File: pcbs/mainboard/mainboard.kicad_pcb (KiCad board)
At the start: 4 copper layers, 49 parts, among them J1 USB_B_Micro, J10 STAT_LED, J11 nReset_Button, J12 VBUS, J2 key_row_0, J3 key_row_1, J4 key_row_2, J5 ICSP, J6 JTAG, J7 Crank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

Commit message: Add first draft of mainboard routing
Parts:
- moved J10 40.7 mm to (116.0, 80.0)
- moved J11 40.7 mm to (153.0, 97.0)
- moved C5 20.7 mm to (122.5, 95.9)
- moved C10 13.0 mm to (106.5, 101.2), turned to 270 degrees
- moved R4 8.45 mm to (140.4, 106.8), turned to 270 degrees
- moved C13 5.91 mm to (137.9, 90.1), turned to 0 degrees
- moved J5 5.79 mm to (139.5, 110.2), turned to 270 degrees
- moved R1 4.82 mm to (155.0, 113.0), turned to 180 degrees
- moved C5 4.61 mm to (114.0, 85.3)
- moved C11 3.57 mm to (120.5, 110.5), turned to 90 degrees
- moved FB1 3.25 mm to (120.8, 114.0)
- moved L1 2.34 mm to (138.1, 86.8), turned to 270 degrees
- moved U2 2.26 mm to (130.4, 111.0)
- moved H1 2.00 mm to (128.5, 34.0)
- moved J1 1.65 mm to (129.0, 118.8)
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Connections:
- net Net-(R2-Pad2) renamed /D+
- net Net-(R3-Pad1) renamed /D-
- U4 pad 12: MISO -> /key_bus0
- U4 pad 13: MOSI -> SCK
- U4 pad 14: SCK -> MOSI
- U4 pad 16: /key_bus0 -> MISO
- U4 pad 18: /key_sel0 -> /key_sel1
- U4 pad 19: /key_sel1 -> /key_sel0
- U4 pad 40: key_row0_7 -> key_row0_6
- U4 pad 41: key_row0_6 -> key_row0_7
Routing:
- net GPIO7: track 0.00 -> 111.1 mm, vias 0 -> 2
- net GPIO6_HWB: track 0.00 -> 102.8 mm, vias 0 -> 1
- net key_row0_0: track 0.00 -> 86.6 mm
- net key_row0_1: track 0.00 -> 78.6 mm
- net VBUS: track 0.00 -> 75.6 mm, vias 0 -> 3
- net key_row1_0: track 0.00 -> 71.8 mm
- net key_row0_2: track 0.00 -> 71.2 mm
- net key_row2_0: track 0.00 -> 69.1 mm
- net STAT_LED: track 0.00 -> 65.6 mm, vias 0 -> 3
- net key_row1_1: track 0.00 -> 64.1 mm
- net key_row2_1: track 0.00 -> 63.6 mm
- net key_row2_2: track 0.00 -> 58.4 mm
- net GPIO5: track 0.00 -> 57.6 mm
- net key_row1_2: track 0.00 -> 57.4 mm
- net key_row0_3: track 0.00 -> 56.7 mm
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- added copper zone on In2.Cu, net +3V3
- added copper zone on In1.Cu, net GND
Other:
- board outline added: 59 x 93 mm

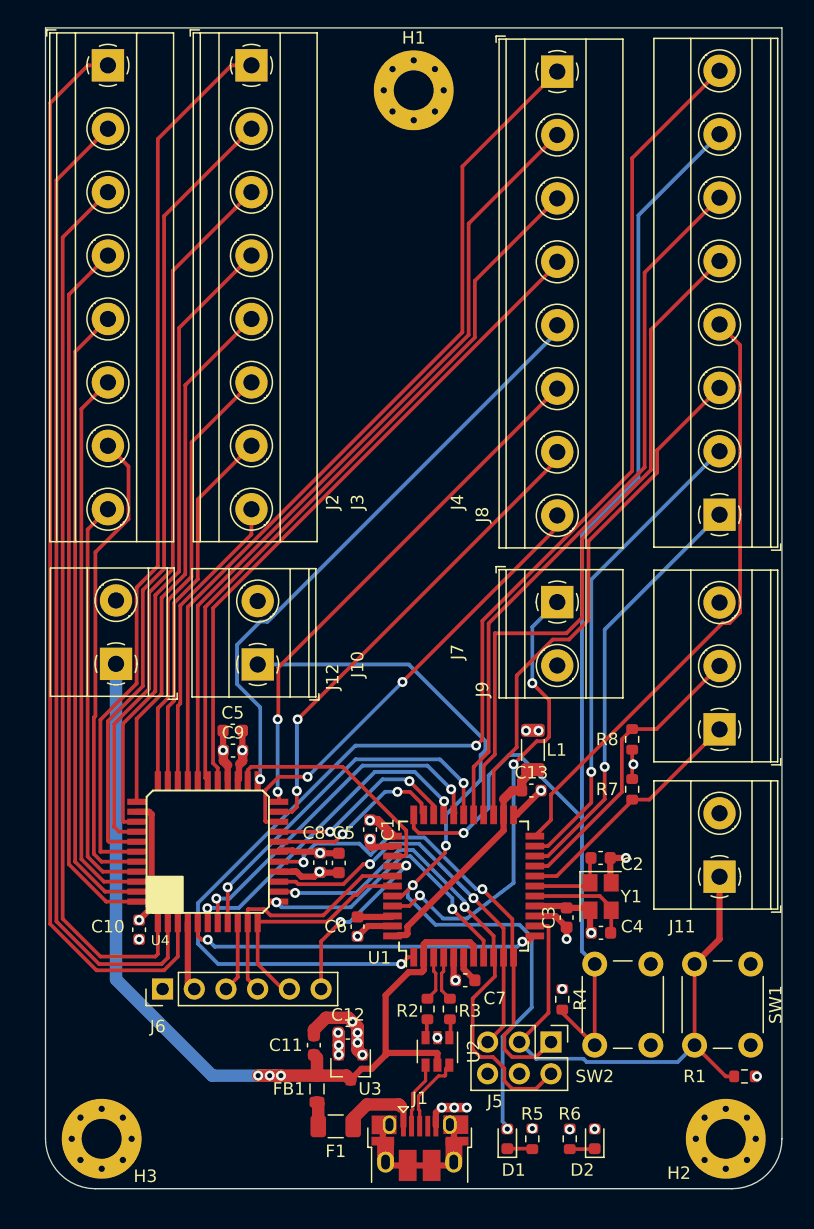
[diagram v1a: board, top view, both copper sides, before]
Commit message: Improve routing around 32U4
Move some pin assignments round on the 32U4 to simplify routing
to the lower-priority IO.
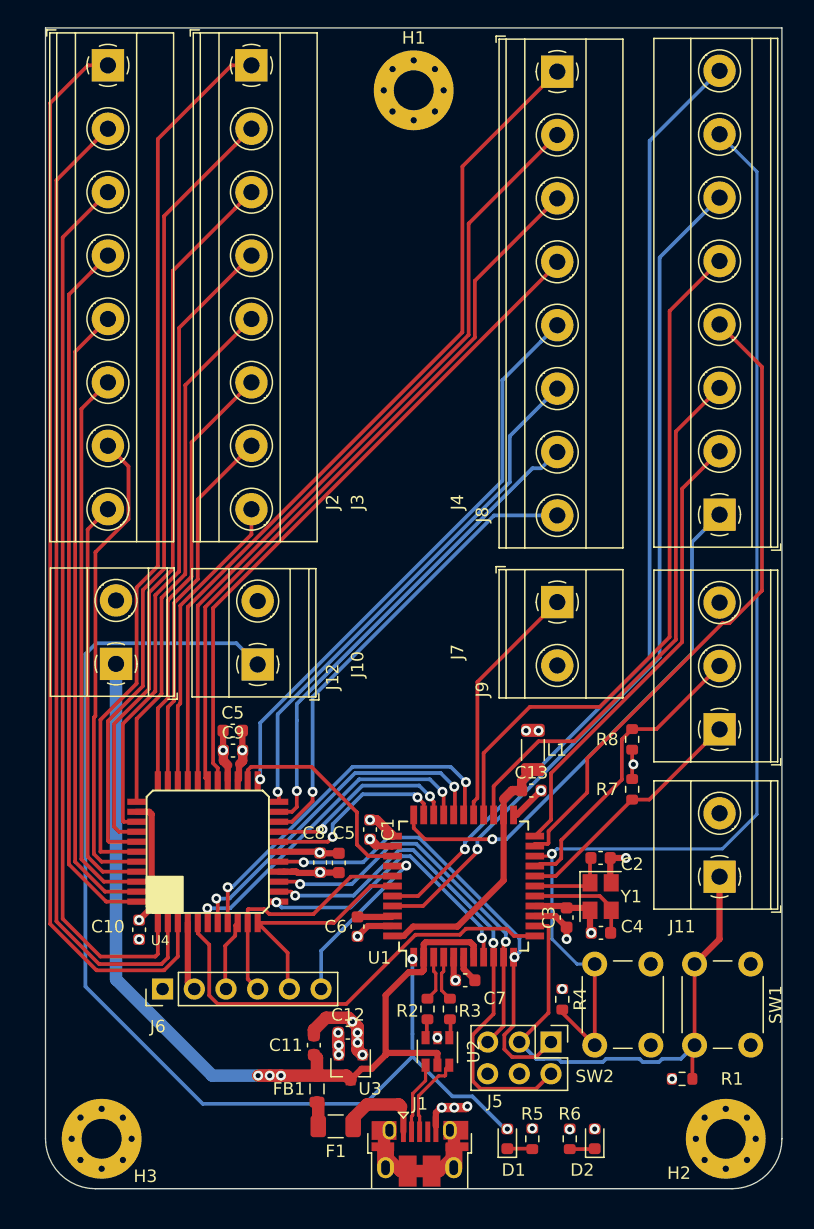
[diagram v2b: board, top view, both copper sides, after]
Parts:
- moved R1 5.00 mm to (150.0, 113.2), turned to 0 degrees
- moved J1 0.45 mm to (129.0, 119.2)
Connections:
- U1 pad 1: GPIO7 -> STAT_LED
- U1 pad 20: GPIO0 -> GPIO6_HWB
- U1 pad 21: GPIO1 -> GPIO3
- U1 pad 22: GPIO3 -> GPIO1
- U1 pad 27: GPIO5 -> CRANK_V_IN
- U1 pad 33: GPIO6_HWB -> GPIO0
- U1 pad 40: STAT_LED -> GPIO7
- U1 pad 41: CRANK_V_IN -> GPIO5
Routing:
- net GPIO7: track 111.1 -> 78.2 mm, vias 2 -> 1
- net STAT_LED: track 65.6 -> 91.2 mm, vias 3 -> 2
- net CRANK_V_IN: track 37.2 -> 19.8 mm, vias 3 -> 0
- net GPIO5: track 57.6 -> 69.0 mm, vias 0 -> 1
- net GPIO0: track 34.1 -> 41.9 mm
- net /key_bus7: track 28.8 -> 35.3 mm, vias 2 -> 0
- net GPIO6_HWB: track 102.8 -> 96.4 mm
- net GPIO3: track 48.8 -> 51.7 mm
- net Net-(J1-Pad6): track 9.36 -> 11.7 mm
- net +3.3VA: track 19.0 -> 21.0 mm
- net 32U4_TDI: track 19.0 -> 17.0 mm
- net key_row2_4: track 48.4 -> 46.5 mm
- net GPIO1: track 38.4 -> 37.0 mm, vias 1 -> 0
- net nReset_32U4: track 45.1 -> 43.9 mm
- net MISO: track 38.6 -> 37.4 mm
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
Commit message: Fix vias placed under SMD pads
Move vias out from underneath SMD pads to prevent solder paste
being sucked into them during manufacture.

Redo power layout to accomadate large areas of vias to power planes.
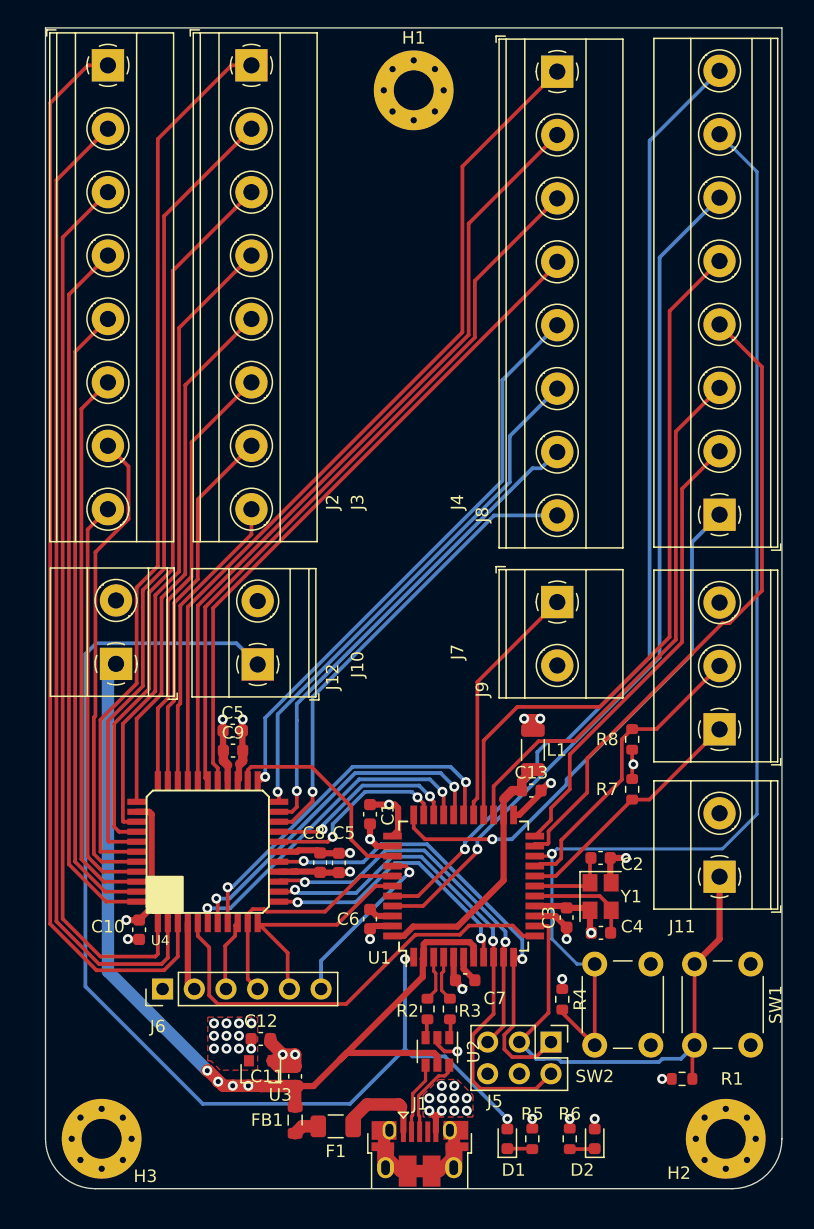
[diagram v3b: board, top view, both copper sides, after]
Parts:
- moved U3 7.21 mm to (116.2, 112.8)
- moved C12 6.99 mm to (116.2, 110.0)
- moved FB1 3.05 mm to (119.0, 116.5)
- moved C11 2.92 mm to (119.0, 113.0)
- moved C1 1.22 mm to (125.0, 92.0)
- moved C6 1.17 mm to (125.0, 100.4)
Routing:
- net +3V3: track 31.7 -> 39.8 mm, vias 14 -> 22
- net GND: track 46.3 -> 53.4 mm, vias 19 -> 24
- net /key_bus0: track 23.3 -> 22.2 mm
- net STAT_LED: track 91.2 -> 92.1 mm
- net GPIO7: track 78.2 -> 79.0 mm
- net AREF: track 2.83 -> 2.02 mm
- net GPIO4: track 55.5 -> 56.1 mm
- net VBUS: track 75.6 -> 76.0 mm, vias 3 -> 4
- added copper zone on F.Cu, net +3V3
- added copper zone on F.Cu, net GND

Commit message: Add useful/readabhle silkscreen
Swap pins on CRANK_V_IN terminal block to shorten track
and match the polarity of other +/- terminal blocks.
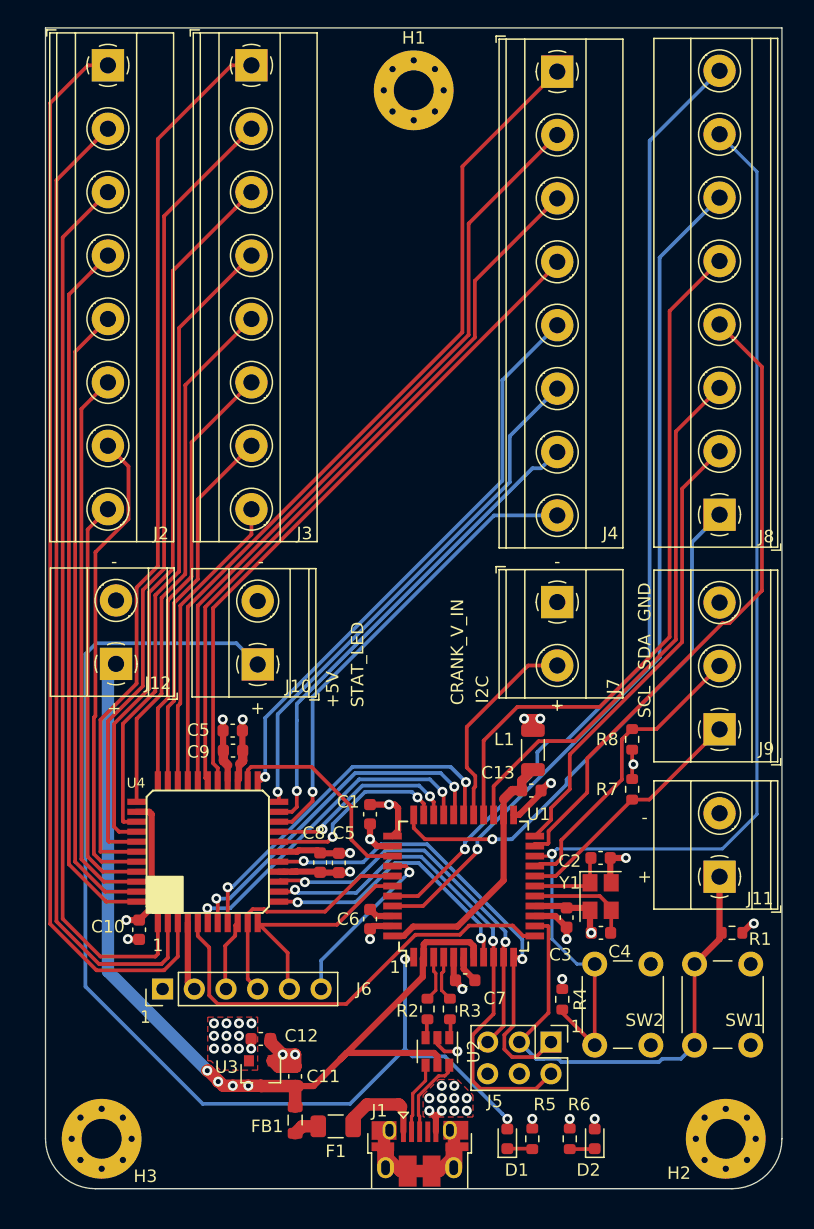
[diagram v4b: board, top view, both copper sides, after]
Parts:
- moved R1 12.4 mm to (154.0, 101.5), turned to 180 degrees
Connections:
- J7 pad 1: CRANK_V_IN -> GND
- J7 pad 2: GND -> CRANK_V_IN
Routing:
- net CRANK_V_IN: track 19.8 -> 17.3 mm
- net nReset_32U4: track 43.7 -> 41.2 mm
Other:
- board text added: "+"
- board text added: "+5V"
- board text added: "-"
- board text added: "1"
- board text added: "CRANK_V_IN"
- board text added: "GND"
- board text added: "I2C"
- board text added: "SCL"
- board text added: "SDA"
- board text added: "STAT_LED"

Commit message: Move H2, H3 up to ease USB port chassis placement
Move mounting holes H2 and H3 up a few mm to allow the USB port to
allow the USB port to be placed as close to the edge of the
chassis as possible.
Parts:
- moved H2 2.00 mm to (153.5, 116.0)
- moved H3 2.00 mm to (103.5, 116.0)
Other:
- board text added: "2"
- board text added: "7"
- board text added: "8"
- board text added: "GPIO"
- board text added: "key_row0"
- board text added: "key_row1"
- board text added: "key_row2"
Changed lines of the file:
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@@
   (general
     (thickness 1.6)
-    (drawings 26)
+    (drawings 38)
     (tracks 707)
     (zones 0)
@@
   )
   (module MountingHole:MountingHole_3.2mm_M3_Pad_Via (layer F.Cu)
-    (at 103.5 118)
+    (at 103.5 116)
     (descr "Mounting Hole 3.2mm, M3")
     (tags "mounting hole 3.2mm m3")
@@
   )
   (module MountingHole:MountingHole_3.2mm_M3_Pad_Via (layer F.Cu)
-    (at 153.5 118)
+    (at 153.5 116)
     (descr "Mounting Hole 3.2mm, M3")
     (tags "mounting hole 3.2mm m3")
@@
     )
   )
+  (gr_text 2 (at 134 62) (layer F.SilkS)
+    (effects (font (size 1 1) (thickness 0.15)))
+  )
+  (gr_text 7 (at 132 62) (layer F.SilkS)
+    (effects (font (size 1 1) (thickness 0.15)))
+  )
+  (gr_text 7 (at 124 62) (layer F.SilkS)
+    (effects (font (size 1 1) (thickness 0.15)))
+  )
+  (gr_text 7 (at 122 62) (layer F.SilkS)
+    (effects (font (size 1 1) (thickness 0.15)))
+  )
+  (gr_text 8 (at 134 31) (layer F.SilkS)
+    (effects (font (size 1 1) (thickness 0.15)))
+  )
+  (gr_text 1 (at 132 31) (layer F.SilkS)
+    (effects (font (size 1 1) (thickness 0.15)))
+  )
+  (gr_text 1 (at 124 31) (layer F.SilkS)
+    (effects (font (size 1 1) (thickness 0.15)))
+  )
+  (gr_text 1 (at 122 31) (layer F.SilkS)
+    (effects (font (size 1 1) (thickness 0.15)))
+  )
+  (gr_text GPIO (at 134 68 90) (layer F.SilkS)
+    (effects (font (size 1 1) (thickness 0.15)))
+  )
+  (gr_text key_row2 (at 132 67 90) (layer F.SilkS)
+    (effects (font (size 1 1) (thickness 0.15)))
+  )
+  (gr_text key_row1 (at 124 67 90) (layer F.SilkS)
+    (effects (font (size 1 1) (thickness 0.15)))
+  )
+  (gr_text key_row0 (at 122 67 90) (layer F.SilkS)
+    (effects (font (size 1 1) (thickness 0.15)))
+  )
   (gr_text GND (at 147 75 90) (layer F.SilkS)
